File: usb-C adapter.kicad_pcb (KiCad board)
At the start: 2 copper layers, 24.6 x 29.5 mm, 20 parts, among them U1 IP2721, U2 LND01

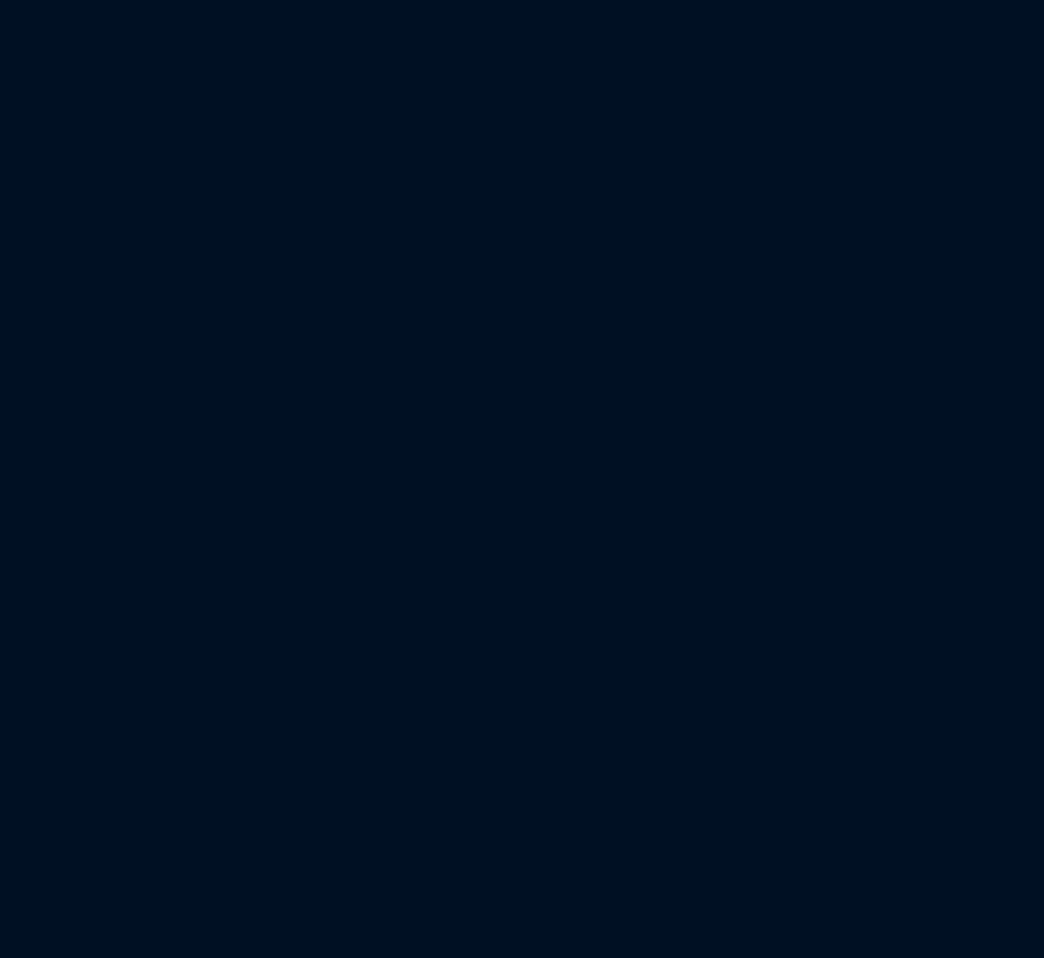
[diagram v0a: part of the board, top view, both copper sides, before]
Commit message: fix(all): combined pcbs
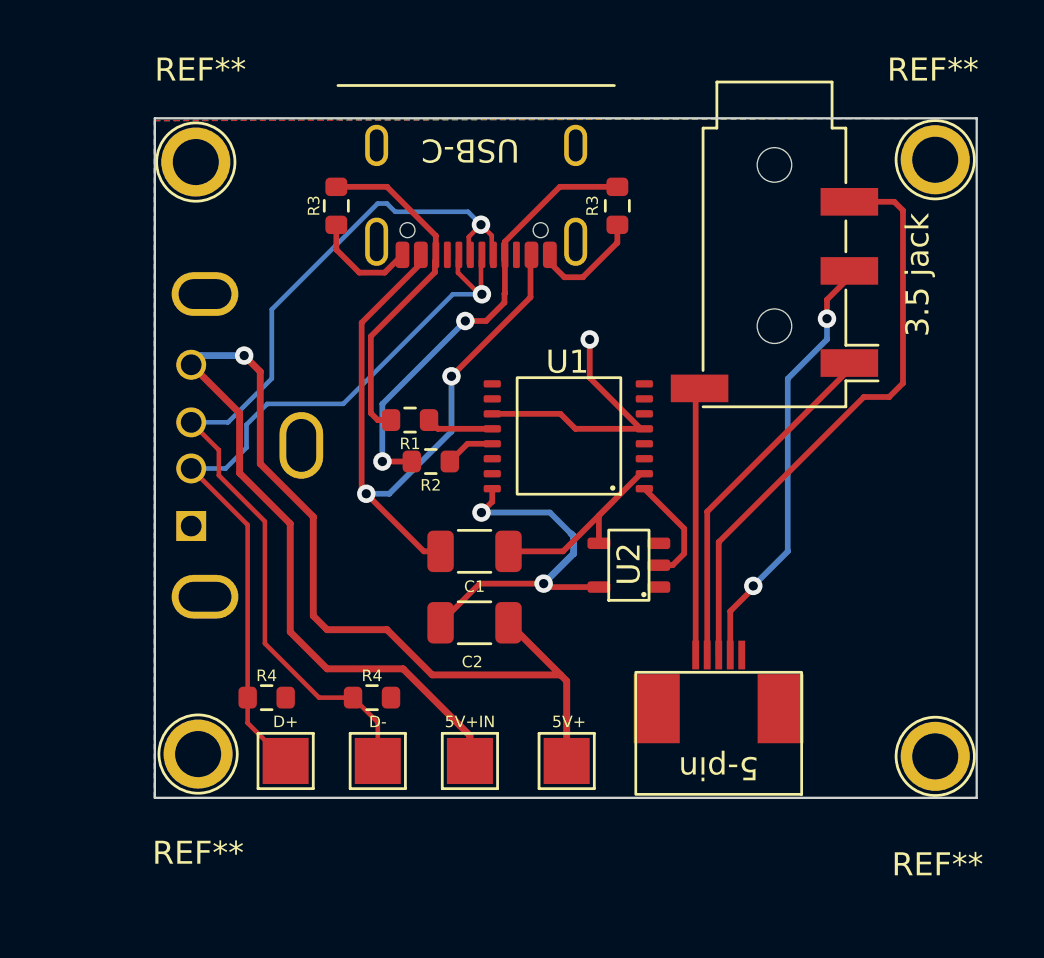
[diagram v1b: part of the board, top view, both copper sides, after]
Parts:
- added 3.5 jack: Jack_3.5mm_PJ320D_Horizontal, Connector_Audio:Jack_3.5mm_PJ320D_Horizontal, F.Cu at (210.7, 77.9)
- added 5-pin: 5pin FPC, ucb-c adapter:5pin FPC, F.Cu at (208.3, 97.8)
- added 5V+: TestPoint_Pad_2.0x2.0mm, TestPoint:TestPoint_Pad_2.0x2.0mm, F.Cu at (201.7, 99.0)
- added 5V+IN: TestPoint_Pad_2.0x2.0mm, TestPoint:TestPoint_Pad_2.0x2.0mm, F.Cu at (197.5, 99.0)
- added C1: C_1206_3216Metric, Capacitor_SMD:C_1206_3216Metric, F.Cu at (197.7, 89.9)
- added C2: C_1206_3216Metric, Capacitor_SMD:C_1206_3216Metric, F.Cu at (197.7, 93.0)
- added D+: TestPoint_Pad_2.0x2.0mm, TestPoint:TestPoint_Pad_2.0x2.0mm, F.Cu at (189.5, 99.0)
- added D-: TestPoint_Pad_2.0x2.0mm, TestPoint:TestPoint_Pad_2.0x2.0mm, F.Cu at (193.5, 99.0)
- added R1: R_0603_1608Metric, Resistor_SMD:R_0603_1608Metric, F.Cu at (194.9, 84.2)
- added R2: R_0603_1608Metric, Resistor_SMD:R_0603_1608Metric, F.Cu at (195.8, 86.0)
- added R3: R_0603_1608Metric, Resistor_SMD:R_0603_1608Metric, F.Cu at (203.9, 74.9)
- added R3: R_0603_1608Metric, Resistor_SMD:R_0603_1608Metric, F.Cu at (191.7, 74.9)
- added R4: R_0603_1608Metric, Resistor_SMD:R_0603_1608Metric, F.Cu at (193.2, 96.2)
- added R4: R_0603_1608Metric, Resistor_SMD:R_0603_1608Metric, F.Cu at (188.7, 96.2)
- added REF**: TestPoint_Plated_Hole_D2.0mm, TestPoint:TestPoint_Plated_Hole_D2.0mm, F.Cu at (217.7, 98.8)
- added REF**: TestPoint_Plated_Hole_D2.0mm, TestPoint:TestPoint_Plated_Hole_D2.0mm, F.Cu at (185.7, 98.7)
- added REF**: TestPoint_Plated_Hole_D2.0mm, TestPoint:TestPoint_Plated_Hole_D2.0mm, F.Cu at (217.7, 72.9)
- added REF**: TestPoint_Plated_Hole_D2.0mm, TestPoint:TestPoint_Plated_Hole_D2.0mm, F.Cu at (185.6, 73.0)
- added U1: IP2721, ucb-c adapter:IP2721, F.Cu at (201.8, 84.9)
- added U2: LND01, ucb-c adapter:LND01, F.Cu at (204.4, 90.5)
- added USB-A: USB_A_Molex_105057_Vertical, Connector_USB:USB_A_Molex_105057_Vertical, B.Cu at (185.4, 88.8)
- added USB-C: usb-c f, ucb-c adapter:usb-c f, F.Cu at (197.8, 73.6)
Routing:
- net 5V+: track 58.0 -> 116.0 mm, vias 1 -> 2
- net VBUS: track 45.1 -> 90.2 mm, vias 4 -> 8
- net D-: track 41.7 -> 83.4 mm, vias 1 -> 2
- net D+: track 34.2 -> 68.4 mm, vias 1 -> 2
- net GND: track 21.4 -> 54.6 mm, vias 1 -> 2
- net HRP: track 0.00 -> 25.5 mm
- net CC1: track 22.4 -> 44.8 mm, vias 2 -> 4
- net HPL: track 0.00 -> 18.9 mm, vias 0 -> 2
- net CC2: track 17.7 -> 35.4 mm
- net HPS: track 0.00 -> 15.3 mm
- net VIN: track 9.31 -> 18.6 mm
- net VBUSG: track 4.84 -> 9.69 mm
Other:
- board size 24.6 x 29.5 mm -> 88.3 x 30.5 mm

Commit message: feat(gerber-files): ready to upload for any pcb website
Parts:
- added G***: LOGO, graphics:iblis 5mm, B.Cu at (152.7, 80.9)
- added G***: LOGO, graphics:iblis 5mm, B.Cu at (213.9, 93.8)
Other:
- board text added: "Made by DDIBLIS"

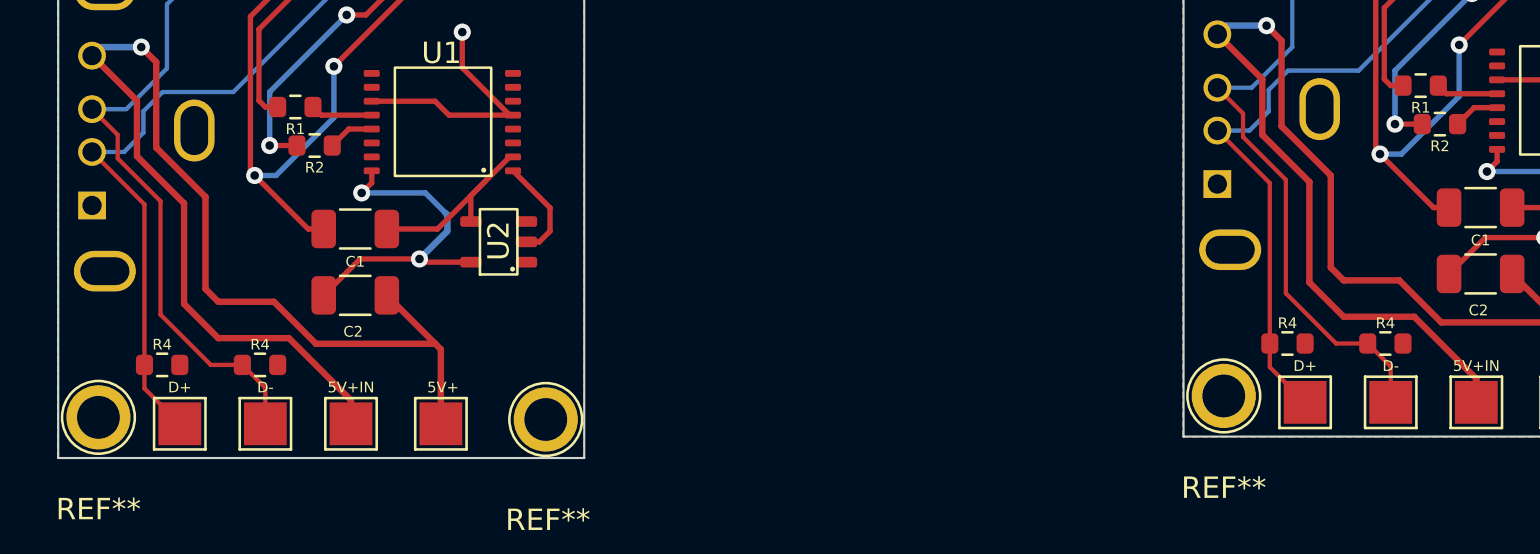
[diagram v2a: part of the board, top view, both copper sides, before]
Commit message: fix(usb-c-adapter): Fixed issue of non grounded resistors
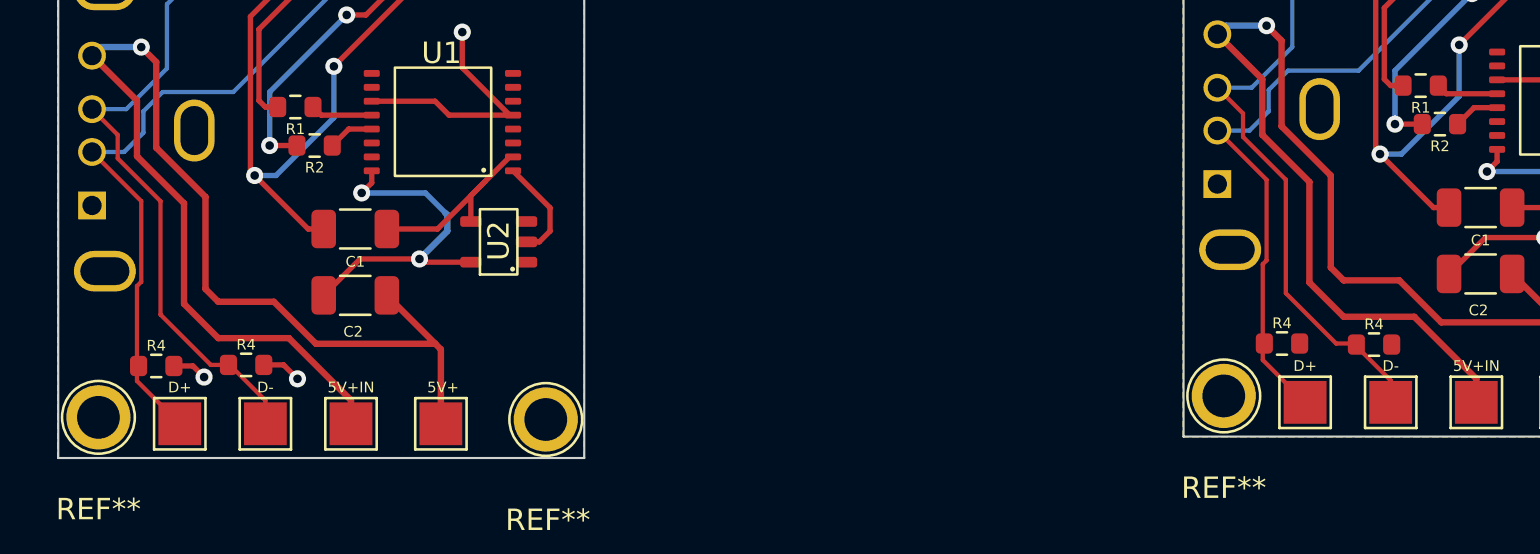
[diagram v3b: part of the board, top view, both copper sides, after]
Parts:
- moved R4 0.65 mm to (140.0, 97.2)
- moved R4 0.53 mm to (192.7, 96.3)
- moved R4 0.28 mm to (135.8, 97.3)
- moved R4 0.25 mm to (188.4, 96.2)
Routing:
- net GND: track 54.6 -> 58.1 mm, vias 2 -> 4
- net D-: track 83.4 -> 82.6 mm

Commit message: feat(no-headphone-usb-c-adapter-shrunk-down): NA
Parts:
- added 5V+: TestPoint_Pad_2.0x2.0mm, TestPoint:TestPoint_Pad_2.0x2.0mm, F.Cu at (194.3, 147.5)
- added 5V+IN: TestPoint_Pad_2.0x2.0mm, TestPoint:TestPoint_Pad_2.0x2.0mm, F.Cu at (190.1, 147.5)
- added C1: C_1206_3216Metric, Capacitor_SMD:C_1206_3216Metric, F.Cu at (187.0, 139.9)
- added C2: C_1206_3216Metric, Capacitor_SMD:C_1206_3216Metric, F.Cu at (187.0, 142.9)
- added D+: TestPoint_Pad_2.0x2.0mm, TestPoint:TestPoint_Pad_2.0x2.0mm, F.Cu at (182.2, 147.5)
- added D-: TestPoint_Pad_2.0x2.0mm, TestPoint:TestPoint_Pad_2.0x2.0mm, F.Cu at (186.0, 147.5)
- added G***: LOGO, graphics:iblis 5mm, B.Cu at (195.5, 136.2)
- added R1: R_0603_1608Metric, Resistor_SMD:R_0603_1608Metric, F.Cu at (186.1, 135.6)
- added R2: R_0603_1608Metric, Resistor_SMD:R_0603_1608Metric, F.Cu at (186.9, 137.3)
- added R3: R_0603_1608Metric, Resistor_SMD:R_0603_1608Metric, F.Cu at (183.6, 129.3)
- added R33: R_0603_1608Metric, Resistor_SMD:R_0603_1608Metric, F.Cu at (195.6, 129.0)
- added R4: R_0603_1608Metric, Resistor_SMD:R_0603_1608Metric, F.Cu at (182.2, 145.2)
- added R4: R_0603_1608Metric, Resistor_SMD:R_0603_1608Metric, F.Cu at (186.0, 145.2)
- added REF**: TestPoint_Plated_Hole_D2.0mm, TestPoint:TestPoint_Plated_Hole_D2.0mm, F.Cu at (178.5, 147.3)
- added REF**: TestPoint_Plated_Hole_D2.0mm, TestPoint:TestPoint_Plated_Hole_D2.0mm, F.Cu at (198.2, 147.4)
- added REF**: TestPoint_Plated_Hole_D2.0mm, TestPoint:TestPoint_Plated_Hole_D2.0mm, F.Cu at (178.5, 126.6)
- added REF**: TestPoint_Plated_Hole_D2.0mm, TestPoint:TestPoint_Plated_Hole_D2.0mm, F.Cu at (198.1, 126.8)
- added U1: IP2721, ucb-c adapter:IP2721, F.Cu at (192.4, 134.8)
- added U2: LND01, ucb-c adapter:LND01, F.Cu at (192.4, 140.9)
- added USB-A: USB_A_Molex_105057_Vertical, Connector_USB:USB_A_Molex_105057_Vertical, B.Cu at (178.3, 140.0)
- added USB-C: usb-c f, ucb-c adapter:usb-c f, F.Cu at (189.6, 127.4)
- renumbered R3 to R33
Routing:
- net 5V+: track 116.0 -> 150.4 mm
- net VBUS: track 90.2 -> 124.3 mm, vias 8 -> 13
- net D-: track 82.6 -> 115.2 mm, vias 2 -> 3
- net D+: track 68.7 -> 97.8 mm, vias 2 -> 3
- net CC1: track 44.8 -> 69.0 mm, vias 4 -> 7
- net GND: track 58.1 -> 80.6 mm, vias 4 -> 9
- net CC2: track 35.4 -> 50.5 mm
- net VIN: track 18.6 -> 29.5 mm
- net VBUSG: track 9.69 -> 14.6 mm
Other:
- board size 88.3 x 30.5 mm -> 88.3 x 78.1 mm

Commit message: build(2.0-build-with-reduced-size-and-cleaned-contact-points): no
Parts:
- added 3.5 jack: Jack_3.5mm_PJ320D_Horizontal, Connector_Audio:Jack_3.5mm_PJ320D_Horizontal, F.Cu at (63.2, 52.8)
- added 5-pin: 5pin FPC, ucb-c adapter:5pin FPC, F.Cu at (63.9, 67.5)
- added 5V+: TestPoint_Pad_2.0x2.0mm, TestPoint:TestPoint_Pad_2.0x2.0mm, F.Cu at (56.1, 68.5)
- added 5V+IN: TestPoint_Pad_2.0x2.0mm, TestPoint:TestPoint_Pad_2.0x2.0mm, F.Cu at (52.0, 68.5)
- added C1: C_1206_3216Metric, Capacitor_SMD:C_1206_3216Metric, F.Cu at (48.9, 61.0)
- added C2: C_1206_3216Metric, Capacitor_SMD:C_1206_3216Metric, F.Cu at (48.9, 63.3)
- added D+: TestPoint_Pad_2.0x2.0mm, TestPoint:TestPoint_Pad_2.0x2.0mm, F.Cu at (44.0, 68.5)
- added D-: TestPoint_Pad_2.0x2.0mm, TestPoint:TestPoint_Pad_2.0x2.0mm, F.Cu at (47.9, 68.5)
- added G***: LOGO, graphics:iblis 5mm, B.Cu at (59.1, 62.0)
- added R1: R_0603_1608Metric, Resistor_SMD:R_0603_1608Metric, F.Cu at (48.0, 56.6)
- added R2: R_0603_1608Metric, Resistor_SMD:R_0603_1608Metric, F.Cu at (48.8, 58.4)
- added R3: R_0603_1608Metric, Resistor_SMD:R_0603_1608Metric, F.Cu at (45.5, 50.4)
- added R33: R_0603_1608Metric, Resistor_SMD:R_0603_1608Metric, F.Cu at (57.5, 50.0)
- added R4: R_0603_1608Metric, Resistor_SMD:R_0603_1608Metric, F.Cu at (44.0, 66.2)
- added R4: R_0603_1608Metric, Resistor_SMD:R_0603_1608Metric, F.Cu at (47.9, 66.2)
- added REF**: TestPoint_Plated_Hole_D2.0mm, TestPoint:TestPoint_Plated_Hole_D2.0mm, F.Cu at (70.1, 47.7)
- added REF**: TestPoint_Plated_Hole_D2.0mm, TestPoint:TestPoint_Plated_Hole_D2.0mm, F.Cu at (70.1, 68.4)
- added REF**: TestPoint_Plated_Hole_D2.0mm, TestPoint:TestPoint_Plated_Hole_D2.0mm, F.Cu at (40.4, 47.6)
- added REF**: TestPoint_Plated_Hole_D2.0mm, TestPoint:TestPoint_Plated_Hole_D2.0mm, F.Cu at (40.4, 68.3)
- added U1: IP2721, ucb-c adapter:IP2721, F.Cu at (54.3, 55.8)
- added U2: LND01, ucb-c adapter:LND01, F.Cu at (54.2, 62.0)
- added USB-A: USB_A_Molex_105057_Vertical, Connector_USB:USB_A_Molex_105057_Vertical, B.Cu at (40.1, 61.0)
- added USB-C: usb-c f, ucb-c adapter:usb-c f, F.Cu at (51.5, 48.4)
- moved C2 181.4 mm to (23.9, 63.4)
- moved 5V+ 181.1 mm to (31.3, 68.6)
- moved 5V+IN 181.1 mm to (27.1, 68.6)
- moved C1 181.1 mm to (24.0, 61.0)
- moved D- 181.1 mm to (23.0, 68.6)
- moved G*** 181.1 mm to (32.5, 57.3)
- moved R1 181.1 mm to (23.1, 56.7)
- moved R2 181.1 mm to (23.9, 58.4)
- moved R3 181.1 mm to (20.6, 50.4)
- moved R4 181.1 mm to (23.0, 66.3)
- moved REF** 181.1 mm to (15.5, 68.4)
- moved REF** 181.1 mm to (15.5, 47.7)
- moved U2 181.1 mm to (29.4, 62.0)
- moved USB-A 181.1 mm to (15.3, 61.1)
- moved USB-C 181.1 mm to (26.6, 48.5)
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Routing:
- net 5V+: track 150.4 -> 222.0 mm
- net VBUS: track 124.3 -> 157.9 mm, vias 13 -> 18
- net D-: track 115.2 -> 147.8 mm, vias 3 -> 4
- net D+: track 97.8 -> 126.9 mm, vias 3 -> 4
- net GND: track 80.6 -> 107.1 mm, vias 9 -> 12
- net CC1: track 69.0 -> 93.2 mm, vias 7 -> 10
- net HRP: track 25.5 -> 44.4 mm
- net CC2: track 50.5 -> 65.6 mm
- net HPL: track 18.9 -> 32.4 mm, vias 2 -> 4
- net VIN: track 29.5 -> 40.3 mm
- net HPS: track 15.3 -> 24.1 mm
- net VBUSG: track 14.6 -> 19.5 mm
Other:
- board size 88.3 x 78.1 mm -> 61.9 x 57.7 mm

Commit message: build(final-push): final push
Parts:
- moved C2 3.34 mm to (26.4, 65.6)
- moved D+ 3.34 mm to (46.5, 70.8)
- moved R2 3.34 mm to (54.1, 29.8)
- moved R4 3.34 mm to (46.5, 68.5)
- moved REF** 3.34 mm to (37.7, 70.8)
- moved U1 3.34 mm to (60.1, 28.7)
- moved U1 3.34 mm to (56.8, 58.1)
- moved U2 3.34 mm to (31.9, 64.3)
- moved USB-C 3.34 mm to (54.0, 50.6)
- moved 5V+ 3.34 mm to (33.8, 42.9)
- moved 5V+IN 3.34 mm to (29.6, 70.9)
- moved C1 3.34 mm to (29.8, 33.8)
- moved R1 3.34 mm to (25.6, 59.0)
- moved R1 3.34 mm to (53.2, 28.0)
- moved R2 3.34 mm to (26.4, 60.7)
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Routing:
- net GND: track 107.1 -> 101.4 mm, vias 12 -> 13
